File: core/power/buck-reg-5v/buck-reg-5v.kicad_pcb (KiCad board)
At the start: 2 copper layers, 34 parts, among them P1 CONN_01X02, P2 CONN_01X02, U1 LM25576, U2 BT151S-500R

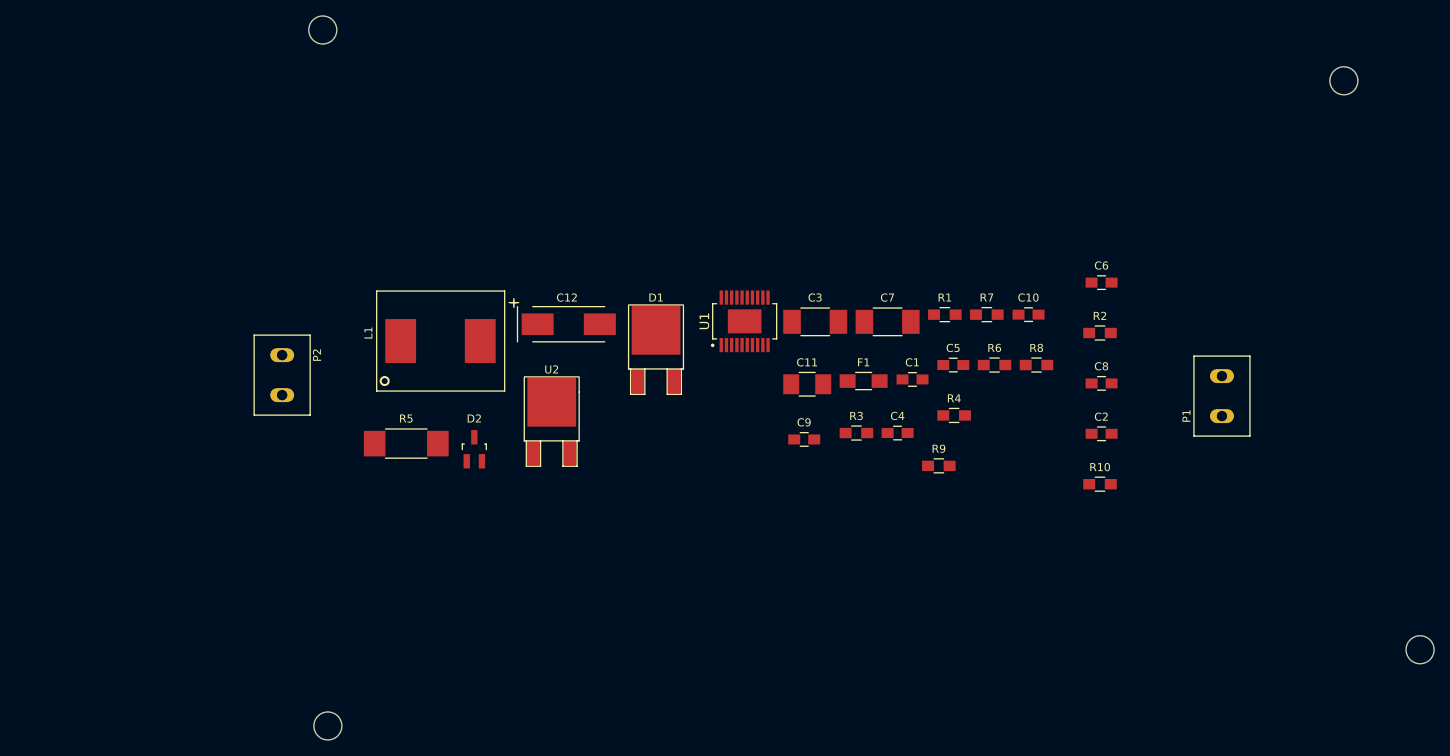
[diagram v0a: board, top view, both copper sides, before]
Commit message: Finished buck reg PCB but needs review (and M3 holes)
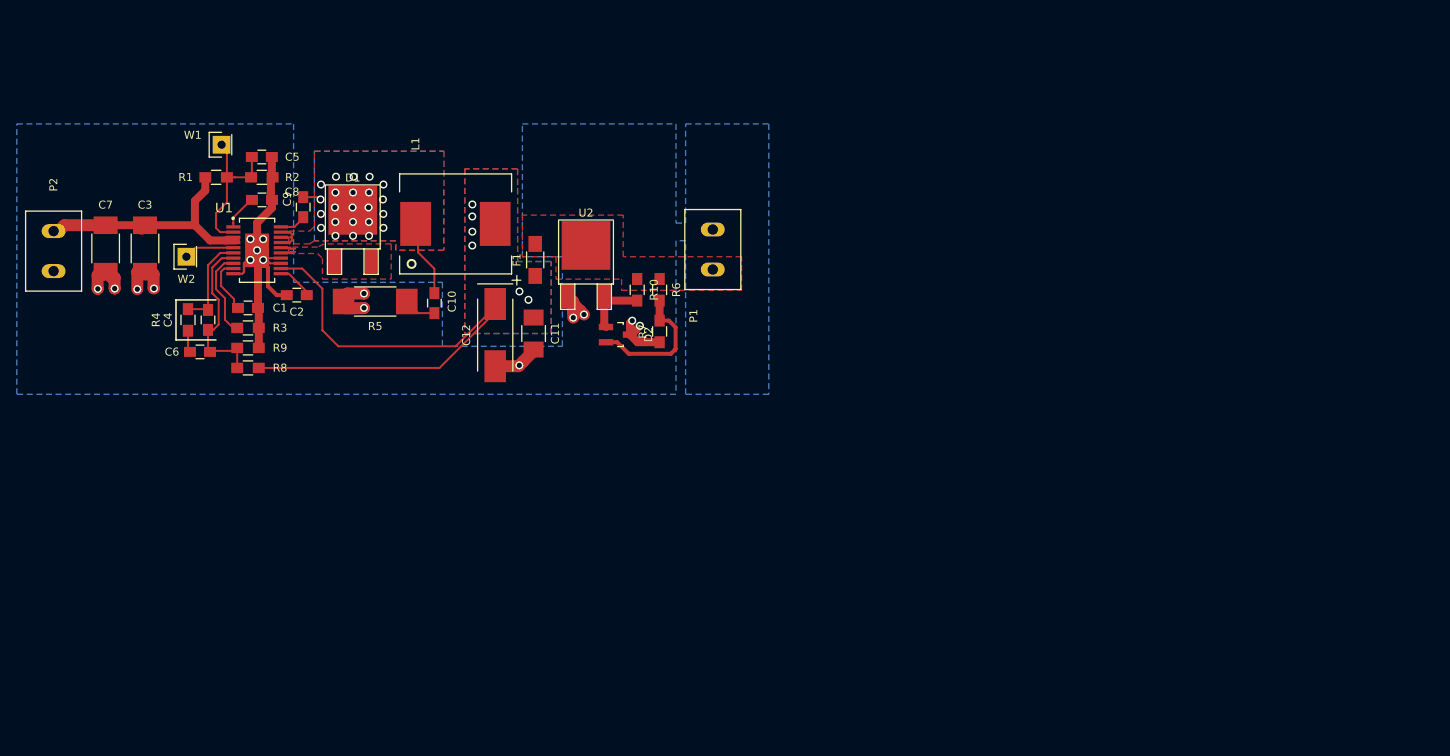
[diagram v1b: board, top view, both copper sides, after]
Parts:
- removed MH1, MH2, MH3, MH4: MOUNTING_HOLE, C-BISCUIT:Mounting_Hole_M3x0.5L_~Plate~_~Pad~
- added W1: TP, Socket_Strips:Socket_Strip_Straight_1x01, F.Cu at (57.2, 62.6)
- added W2: TP, Socket_Strips:Socket_Strip_Straight_1x01, F.Cu at (52.8, 76.6)
- moved C6 113.0 mm to (54.5, 88.5)
- moved C8 107.4 mm to (62.2, 69.5)
- moved R2 106.6 mm to (62.2, 66.7)
- moved C2 102.1 mm to (66.6, 81.4), turned to 180 degrees
- moved R8 98.6 mm to (60.5, 90.5), turned to 180 degrees
- moved C7 98.2 mm to (42.7, 75.6), turned to 270 degrees
- moved R4 96.5 mm to (53.0, 84.5), turned to 270 degrees
- moved R1 92.7 mm to (56.5, 66.7)
- moved C5 90.3 mm to (62.2, 64.1)
- moved R9 87.6 mm to (60.5, 88.0)
- moved C4 87.4 mm to (55.5, 84.5), turned to 270 degrees
- moved C3 84.3 mm to (47.6, 75.6), turned to 270 degrees
- moved C1 83.5 mm to (60.5, 83.0), turned to 180 degrees
- moved R3 77.2 mm to (60.5, 85.5)
- moved C10 74.3 mm to (83.8, 82.4), turned to 90 degrees
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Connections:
- net /REG_OUT renamed /OUT
- net Net-(C1-Pad2) renamed /RAMP
- net Net-(C2-Pad1) renamed /SS
- net Net-(C4-Pad1) renamed /COMP
- net Net-(C4-Pad2) renamed /FB
- net Net-(C5-Pad1) renamed /SD
- net Net-(C8-Pad1) renamed /VCC
- net Net-(C9-Pad2) renamed /BST
- net Net-(R3-Pad1) renamed /RT
- C10 pad 2: Net-(C10-Pad2) -> /SW
- C9 pad 1: Net-(C10-Pad2) -> /SW
- D1 pad 1: Net-(C10-Pad2) -> /IS
- D1 pad 2: Net-(D1-Pad2) -> /SW
- D1 pad 3: (no net) -> /IS
- L1 pad 1: Net-(C10-Pad2) -> /SW
- U1 pad 15: Net-(D1-Pad2) -> /IS
- U1 pad 16: Net-(D1-Pad2) -> /IS
- U1 pad 17: Net-(C10-Pad2) -> /SW
- U1 pad 18: Net-(C10-Pad2) -> /SW
- U1 pad 19: Net-(C10-Pad2) -> /SW
- U1 pad 5: Net-(U1-Pad5) -> /SYNC
- U1 pad EP: (no net) -> GND
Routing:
- net GND: track 0.00 -> 83.6 mm, vias 0 -> 16
- net /OUT: track 0.00 -> 69.7 mm, vias 0 -> 6
- net /BAT_IN: track 0.00 -> 32.4 mm
- net /FB: track 0.00 -> 21.0 mm
- net /SD: track 0.00 -> 19.2 mm
- net /SW: track 0.00 -> 18.5 mm, vias 0 -> 23
- net Net-(D2-Pad2): track 0.00 -> 17.1 mm
- net /COMP: track 0.00 -> 11.9 mm
- net /RT: track 0.00 -> 10.5 mm
- net Net-(D2-Pad1): track 0.00 -> 8.28 mm
- net /RAMP: track 0.00 -> 6.90 mm
- net /SYNC: track 0.00 -> 6.33 mm
- net Net-(C10-Pad1): track 0.00 -> 5.46 mm
- net /SS: track 0.00 -> 4.60 mm
- net /VCC: track 0.00 -> 4.42 mm
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- added copper zone on F.Cu, net +5V
- added copper zone on F.Cu, net /IS
- added copper zone on B.Cu, net /OUT
- added copper zone on F.Cu, net /OUT
- added copper zone on B.Cu, net /SW
- added copper zone on F.Cu, net /SW
- added copper zone on B.Cu, net GND

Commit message: Finished buck reg. Awaiting review
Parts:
- added C13: 150uF, Capacitors_Tantalum_SMD:TantalC_SizeD_EIA-7343_HandSoldering, F.Cu at (97.0, 84.2)
- added REF**: MountingHole_3mm, Mounting_Holes:MountingHole_3mm, F.Cu at (35.8, 64.4)
- added REF**: MountingHole_3mm, Mounting_Holes:MountingHole_3mm, F.Cu at (35.8, 90.0)
- added REF**: MountingHole_3mm, Mounting_Holes:MountingHole_3mm, F.Cu at (121.6, 89.8)
- added REF**: MountingHole_3mm, Mounting_Holes:MountingHole_3mm, F.Cu at (121.6, 64.2)
- moved R7 10.2 mm to (115.6, 76.4)
- moved C11 9.90 mm to (86.4, 84.8)
- moved D2 8.85 mm to (111.3, 78.8)
- moved R10 7.35 mm to (109.6, 73.4)
- moved R6 7.35 mm to (112.4, 73.4)
- moved P1 6.16 mm to (122.2, 73.2), turned to 270 degrees
- moved F1 5.10 mm to (97.4, 72.0)
- moved C10 4.92 mm to (81.6, 78.0), turned to 0 degrees
- moved U2 3.67 mm to (104.6, 78.3)
- moved L1 2.90 mm to (81.6, 69.6)
- moved C12 2.24 mm to (91.0, 84.2)
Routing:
- net /SW: track 18.5 -> 64.8 mm, vias 23 -> 20
- net +5V: track 0.00 -> 23.5 mm, vias 0 -> 12
- net GND: track 83.6 -> 105.7 mm, vias 16 -> 21
- net /OUT: track 69.7 -> 84.6 mm, vias 6 -> 11
- net Net-(D2-Pad1): track 8.28 -> 6.32 mm
- net Net-(C10-Pad1): track 5.46 -> 4.20 mm
- net Net-(D2-Pad2): track 17.1 -> 17.8 mm
- net (no net): vias 0 -> 2
- added copper zone on B.Cu, net +5V

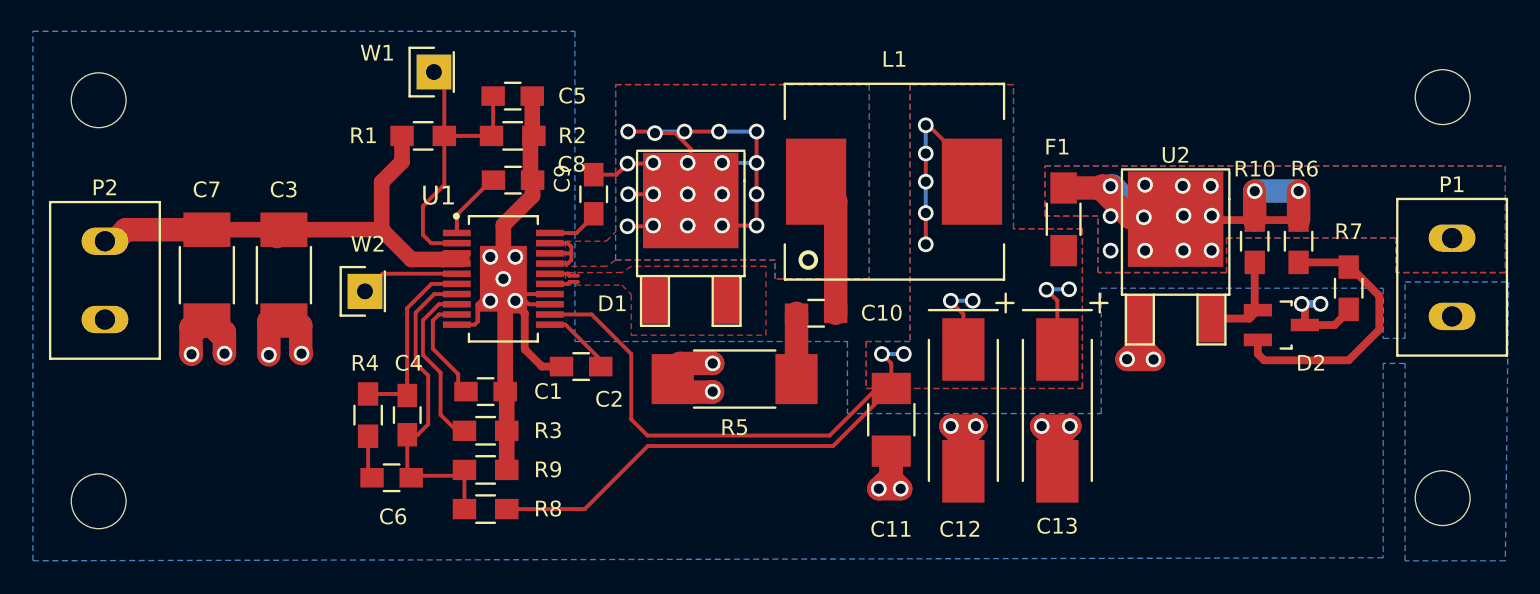
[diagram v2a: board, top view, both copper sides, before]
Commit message: Added mfg files. Still needs links to parts.
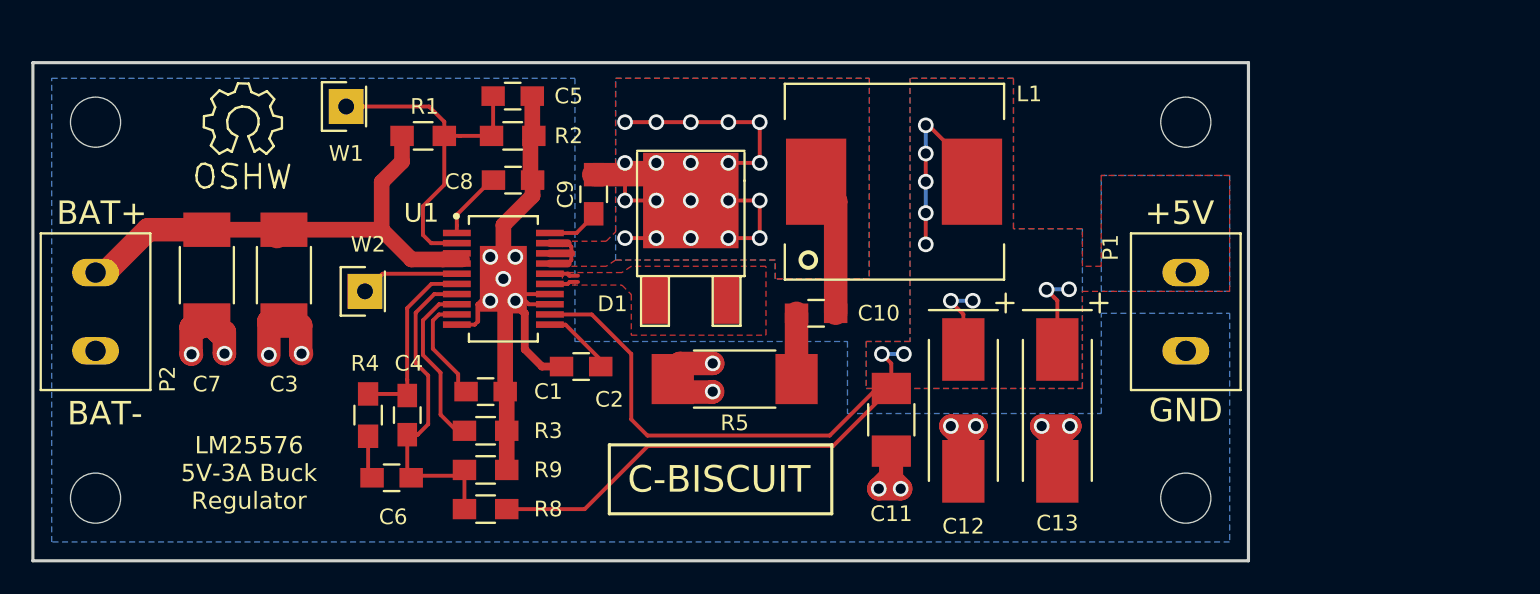
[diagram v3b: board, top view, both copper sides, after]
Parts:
- removed D2: LM431, TO_SOT_Packages_SMD:SOT-23_Handsoldering
- removed F1: 3A, Resistors_SMD:R_1206_HandSoldering
- removed R10: 220, Resistors_SMD:R_0805_HandSoldering
- removed R6: 3.48K, Resistors_SMD:R_0805_HandSoldering
- removed R7: 2.49K, Resistors_SMD:R_0805_HandSoldering
- removed the REF** at (35.8, 64.4)
- removed the REF** at (35.8, 90.0)
- removed the REF** at (121.6, 89.8)
- removed the REF** at (121.6, 64.2)
- removed U2: BT151S-500R, TO_SOT_Packages_SMD:TO-252-2Lead
- added REF**: MountingHole_3mm, Mounting_Holes:MountingHole_3mm, F.Cu at (35.6, 89.8)
- added REF**: MountingHole_3mm, Mounting_Holes:MountingHole_3mm, F.Cu at (35.6, 65.8)
- added REF**: MountingHole_3mm, Mounting_Holes:MountingHole_3mm, F.Cu at (105.2, 89.8)
- added REF**: MountingHole_3mm, Mounting_Holes:MountingHole_3mm, F.Cu at (105.2, 65.8)
- added REF**: Symbol_OSHW-Logo_SilkScreen, Symbols:Symbol_OSHW-Logo_SilkScreen, F.Cu at (45.0, 65.8)
- moved P1 17.1 mm to (105.2, 75.4)
- moved W1 6.02 mm to (51.6, 64.8)
- moved P2 2.09 mm to (35.6, 75.4)
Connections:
- C11 pad 1: /OUT -> +5V
- C12 pad 1: /OUT -> +5V
- C13 pad 1: /OUT -> +5V
- L1 pad 2: /OUT -> +5V
- R8 pad 1: /OUT -> +5V
- U1 pad 12: /OUT -> +5V
- U1 pad EP: GND -> (no net)
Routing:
- net /OUT: track 84.6 -> 0.00 mm, vias 11 -> 0
- net +5V: track 23.5 -> 84.6 mm, vias 12 -> 11
- net Net-(D2-Pad2): track 17.8 -> 0.00 mm
- net GND: track 105.7 -> 92.0 mm, vias 21 -> 17
- net Net-(D2-Pad1): track 6.32 -> 0.00 mm
- net /SD: track 19.2 -> 22.4 mm
- net /BAT_IN: track 32.4 -> 33.8 mm
- net /SW: track 64.8 -> 64.2 mm
- net (no net): vias 2 -> 0
- removed copper zone on B.Cu, net /OUT
- removed copper zone on F.Cu, net /OUT
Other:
- board outline added: 77.6 x 31.8 mm
- board text added: "+5V"
- board text added: "BAT+"
- board text added: "BAT-"
- board text added: "C-BISCUIT"
- board text added: "GND"
- board text added: "LM25576 5V-3A Buck Regulator"
- board text added: "Patrick Lloyd Trevor Gamblin Nick Bentzen"
